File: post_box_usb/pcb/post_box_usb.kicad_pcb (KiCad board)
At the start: 4 copper layers, 90 x 45 mm, 100 parts, among them U1 MCP1700T-3302E/MB, X1 MC146 32768Hz

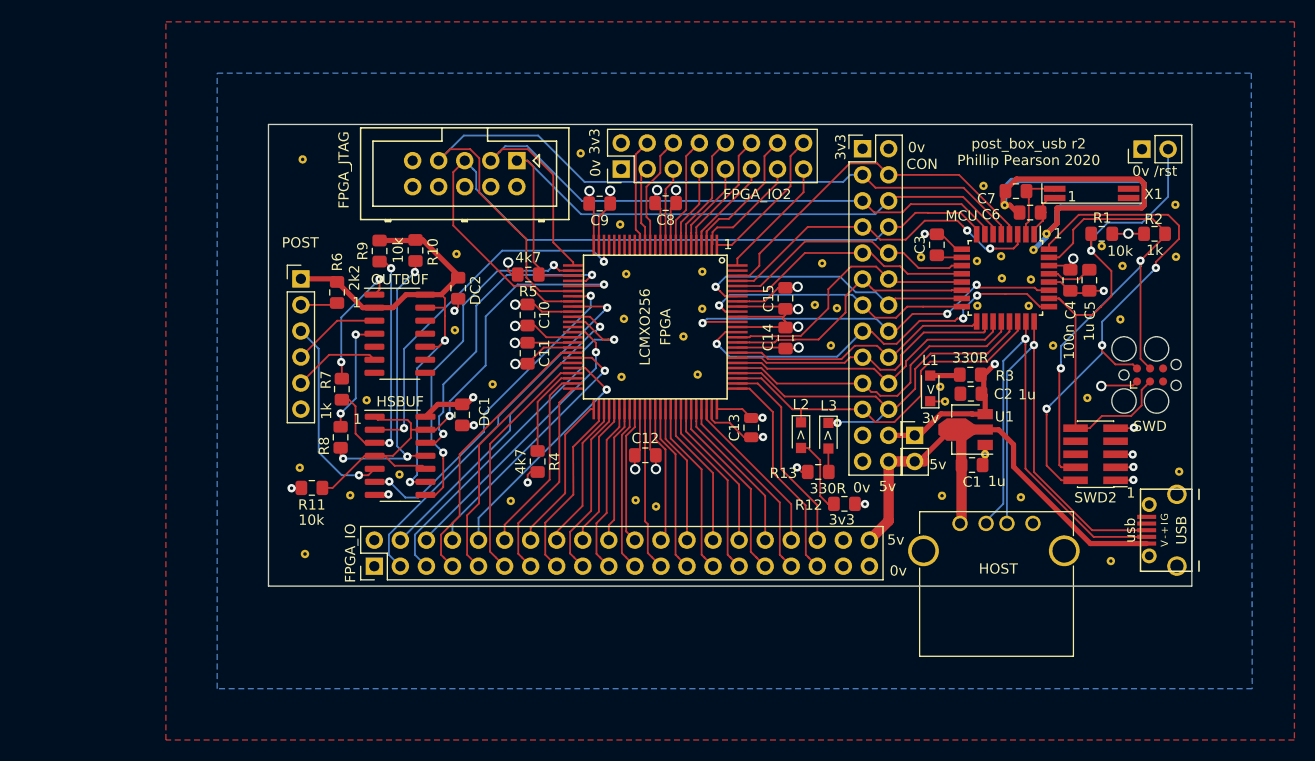
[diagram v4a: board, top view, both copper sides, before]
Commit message: post_box_usb: r2 with an attempt at reverse polarity protection
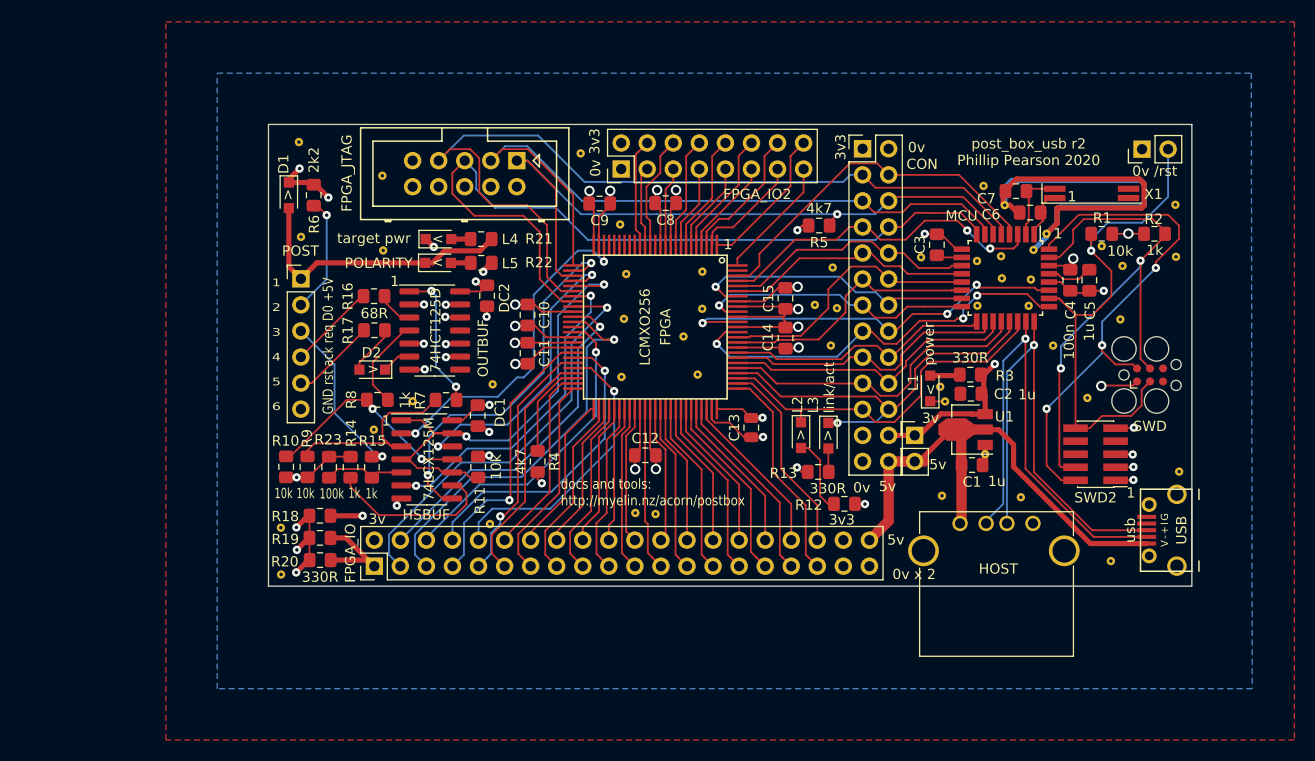
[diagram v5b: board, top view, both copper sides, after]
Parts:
- added D1: BAT54, Diode_SMD:D_SOD-323_HandSoldering, F.Cu at (112.0, 136.9)
- added D2: BAT54, Diode_SMD:D_SOD-323_HandSoldering, F.Cu at (120.1, 153.9)
- added L4: target pwr, Diode_SMD:D_SOD-323_HandSoldering, F.Cu at (126.6, 141.2)
- added L5: POLARITY, Diode_SMD:D_SOD-323_HandSoldering, F.Cu at (126.5, 143.5)
- added R14: 1k, Resistor_SMD:R_0805_2012Metric_Pad1.15x1.40mm_HandSolder, F.Cu at (118.0, 163.4)
- added R15: 1k, Resistor_SMD:R_0805_2012Metric_Pad1.15x1.40mm_HandSolder, F.Cu at (120.1, 163.4)
- added R16: 68R, Resistor_SMD:R_0805_2012Metric_Pad1.15x1.40mm_HandSolder, F.Cu at (120.3, 146.7)
- added R17: 68R, Resistor_SMD:R_0805_2012Metric_Pad1.15x1.40mm_HandSolder, F.Cu at (120.3, 150.1)
- added R18: 330R, Resistor_SMD:R_0805_2012Metric_Pad1.15x1.40mm_HandSolder, F.Cu at (115.0, 168.1)
- added R19: 330R, Resistor_SMD:R_0805_2012Metric_Pad1.15x1.40mm_HandSolder, F.Cu at (115.0, 170.3)
- added R20: 330R, Resistor_SMD:R_0805_2012Metric_Pad1.15x1.40mm_HandSolder, F.Cu at (115.0, 172.5)
- added R21: 330R, Resistor_SMD:R_0805_2012Metric_Pad1.15x1.40mm_HandSolder, F.Cu at (130.7, 141.2)
- added R22: 330R, Resistor_SMD:R_0805_2012Metric_Pad1.15x1.40mm_HandSolder, F.Cu at (130.7, 143.5)
- added R23: 100k, Resistor_SMD:R_0805_2012Metric_Pad1.15x1.40mm_HandSolder, F.Cu at (115.9, 163.4)
- L1: value led -> power
- L3: value led -> link/act
- moved staple_single25 31.7 mm to (113.0, 131.7)
- moved R5 28.8 mm to (163.7, 139.9)
- moved R10 24.6 mm to (111.7, 163.4), turned to 270 degrees
- moved R9 22.2 mm to (113.8, 163.4), turned to 270 degrees
- moved staple_single24 18.9 mm to (111.2, 173.9)
- moved R11 16.3 mm to (130.4, 163.4), turned to 90 degrees
- moved staple_single33 15.3 mm to (113.2, 141.0)
- moved staple_single28 11.0 mm to (124.0, 157.0)
- moved staple_single32 10.5 mm to (121.2, 142.3)
- moved R7 10.2 mm to (127.3, 156.9), turned to 0 degrees
- moved R6 9.75 mm to (114.4, 136.9)
- moved staple_single23 7.93 mm to (121.1, 135.0)
- moved R8 5.12 mm to (120.6, 156.8), turned to 0 degrees
- moved staple_single31 5.03 mm to (120.3, 159.8)
- moved staple_single21 3.48 mm to (111.2, 169.3)
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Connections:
- DC2 pad 1: GND -> target_GND
- HSBUF pad 5: testreq -> target_testreq
- HSBUF pad 9: target_5V -> target_5V_r
- OUTBUF pad 12: GND -> target_GND
- OUTBUF pad 3: testack -> target_testack
- OUTBUF pad 5: GND -> target_GND
- OUTBUF pad 7: GND -> target_GND
- OUTBUF pad 9: GND -> target_GND
- POST pad 1: target_5V -> target_5V_ext
- POST pad 3: testreq -> target_testreq_ext
- POST pad 4: testack -> target_testack_ext
- POST pad 5: target_reset -> target_reset_ext
- POST pad 6: GND -> target_GND
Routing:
- net target_5V: track 52.5 -> 22.8 mm, vias 2 -> 7
- net target_5V_ext: track 0.00 -> 27.6 mm
- net testreq: track 19.2 -> 0.00 mm, vias 1 -> 0
- net target_GND: track 0.00 -> 18.8 mm, vias 0 -> 10
- net target_testreq_ext: track 0.00 -> 17.0 mm, vias 0 -> 1
- net target_5V_r: track 0.00 -> 16.6 mm
- net GND: track 132.3 -> 143.1 mm
- net target_reset_noe_buf: track 29.5 -> 20.7 mm, vias 3 -> 2
- net testack: track 8.63 -> 0.00 mm
- net target_testack_ext: track 0.00 -> 8.56 mm
- net target_reset_ext: track 0.00 -> 8.31 mm
- net target_testreq: track 0.00 -> 7.96 mm
- net target_D0: track 3.60 -> 11.4 mm, vias 0 -> 1
- net testack_noe_buf: track 26.4 -> 19.1 mm, vias 2 -> 0
- net target_reset: track 8.51 -> 2.89 mm
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- added copper zone on In2.Cu, net target_5V
- added copper zone on In1.Cu, net target_GND
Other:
- board text added: "0v x 2"
- board text added: "1 2 3 4 5 6"
- board text added: "<"
- board text added: "GND rst ack req D0 +5V"
- board text added: "docs and tools: http://myelin.nz/acorn/postbox"
- board text added: "post_box_usb r2 Copyright 2017-2020 Google Inc Designed by Phillip Pearson github.com/google/myelin-acorn-electron-hardware myelin.nz/acorn/postbox"
- board text removed: "post_box_usb r1 Copyright 2017-2020 Google Inc Designed by Phillip Pearson github.com/google/myelin-acorn-electron-hardware myelin.nz/acorn/postbox"

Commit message: post_box_usb: r3 candidate; resistors tweaked, diode replaced with mosfet, footprints fixed, test points added
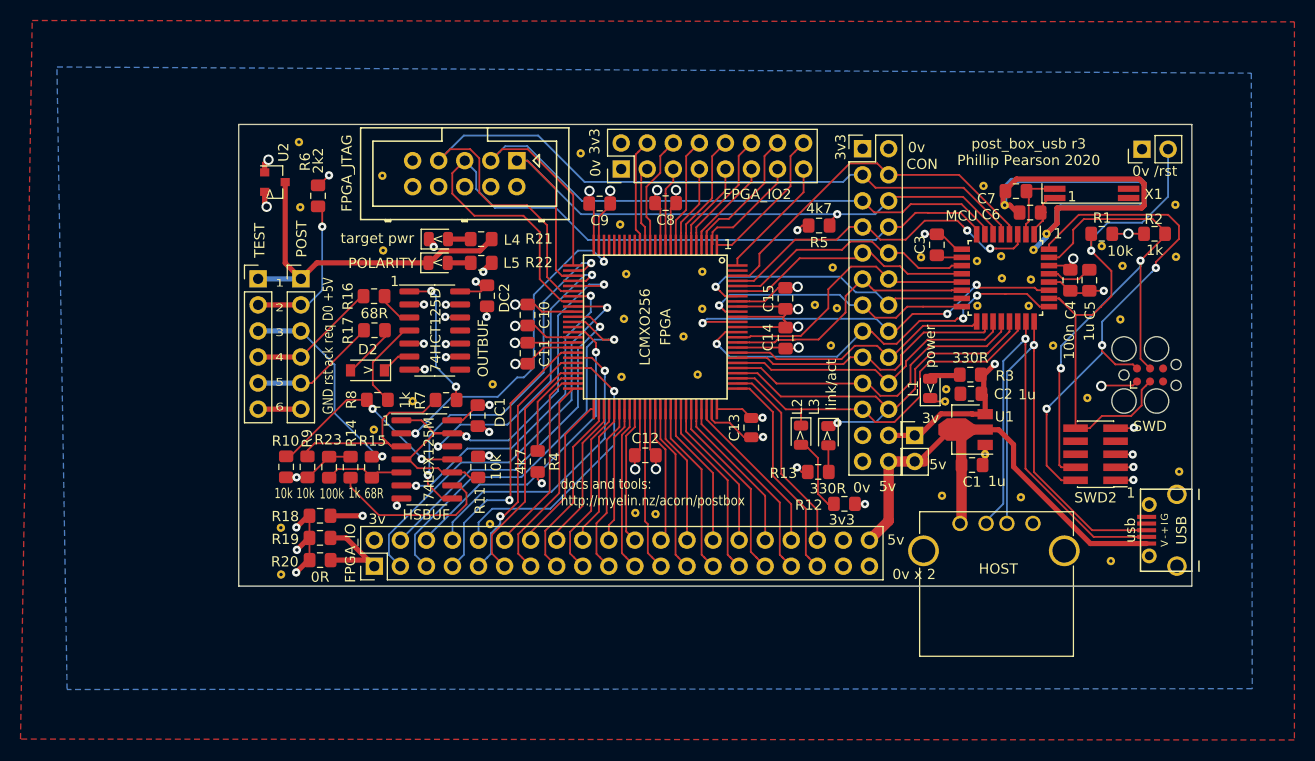
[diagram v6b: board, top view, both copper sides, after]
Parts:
- removed D1: BAT54, Diode_SMD:D_SOD-323_HandSoldering
- added TEST: pins, Connector_PinHeader_2.54mm:PinHeader_1x06_P2.54mm_Vertical, F.Cu at (109.0, 145.1)
- added U2: PMV65XP,215, Package_TO_SOT_SMD:SOT-23, F.Cu at (110.6, 135.6)
- D2: footprint Diode_SMD:D_SOD-323_HandSoldering -> Diode_SMD:D_SOD-123
- L1, L2, L3, L4, L5: footprint Diode_SMD:D_SOD-323_HandSoldering -> LED_SMD:LED_0805_2012Metric
- R15: value 1k -> 68R
- R20: value 330R -> 0R
- moved staple_single33 2.89 mm to (113.1, 138.1)
- moved staple_single20 0.63 mm to (176.1, 155.8)
- moved D2 0.47 mm to (119.7, 154.0)
- moved R6 0.42 mm to (114.8, 137.0)
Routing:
- net target_5V_ext: track 27.6 -> 34.4 mm
- net target_GND: track 18.8 -> 24.2 mm, vias 10 -> 11
- net target_testreq_ext: track 17.0 -> 21.2 mm
- net target_testack_ext: track 8.56 -> 12.7 mm
- net target_reset_ext: track 8.31 -> 12.5 mm
- net target_D0: track 11.4 -> 15.2 mm
- net target_5V: track 22.8 -> 19.5 mm
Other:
- board size 90 x 45 mm -> 92.9 x 45 mm
- board text added: "post_box_usb r3 Copyright 2017-2020 Google Inc Designed by Phillip Pearson github.com/google/myelin-acorn-electron-hardware myelin.nz/acorn/postbox"
- board text added: "post_box_usb r3 Phillip Pearson 2020"
- board text removed: "post_box_usb r2 Copyright 2017-2020 Google Inc Designed by Phillip Pearson github.com/google/myelin-acorn-electron-hardware myelin.nz/acorn/postbox"
- board text removed: "post_box_usb r2 Phillip Pearson 2020"

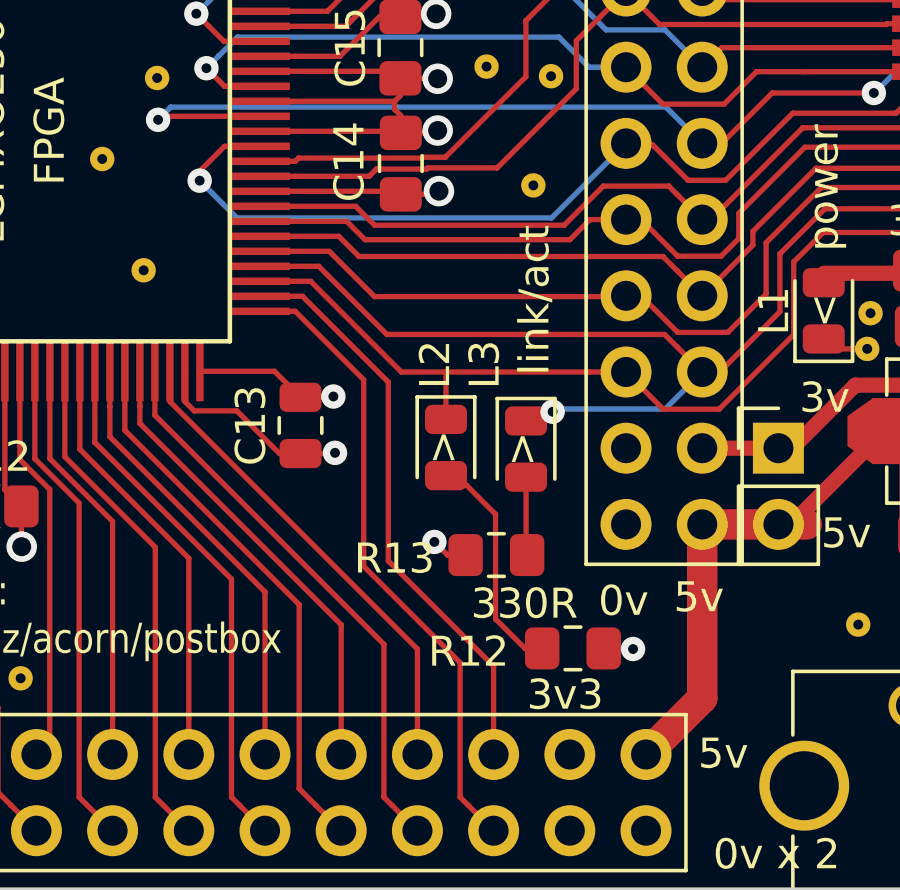
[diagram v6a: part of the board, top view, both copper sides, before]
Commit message: post_box_usb: Replaced L2 with an WS2812-V5
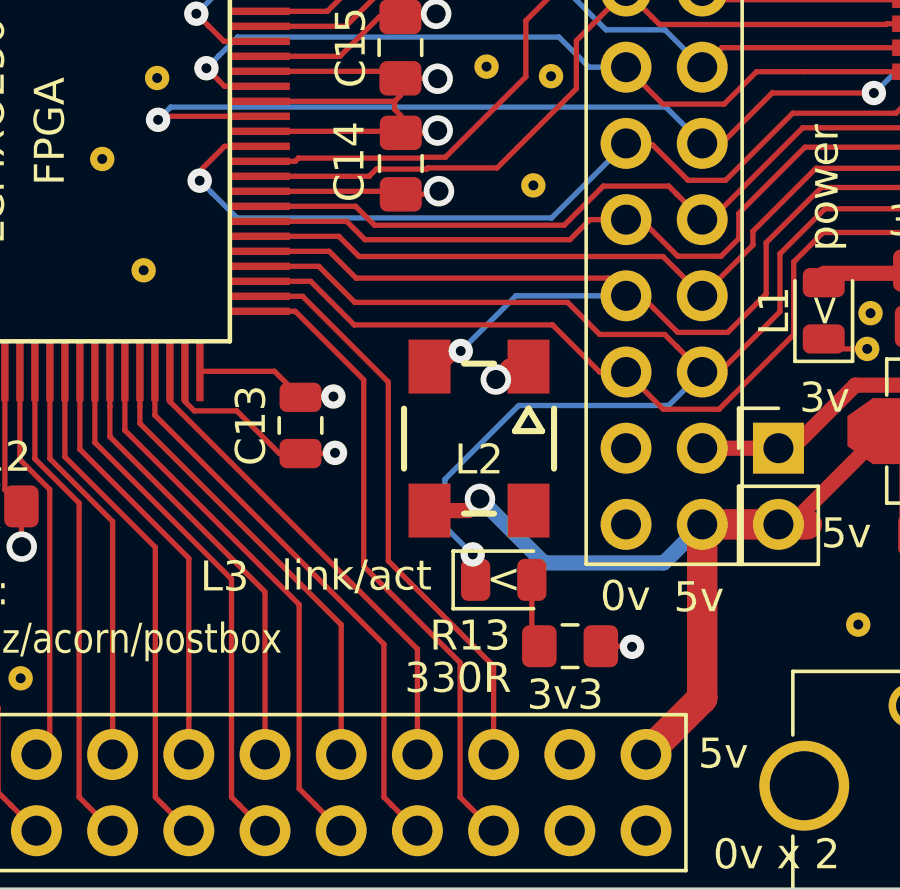
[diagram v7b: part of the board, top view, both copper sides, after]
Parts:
- removed R12: 330R, Resistor_SMD:R_0805_2012Metric_Pad1.15x1.40mm_HandSolder
- L2: value led -> WS2812B-V5; footprint LED_SMD:LED_0805_2012Metric -> myelin-kicad:WS2812B_PP
- R18, R19: value 330R -> 0R NF
- moved L3 4.42 mm to (163.8, 164.7), turned to 0 degrees
- moved R13 3.91 mm to (166.0, 166.9), turned to 180 degrees
- moved L2 1.14 mm to (163.0, 160.0), turned to 0 degrees
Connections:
- L2 pad 1: mcu_RXD -> 5V
- L2 pad 2: mcu_txd_led_anode -> (no net)
- L3 pad 2: mcu_rxd_led_anode -> mcu_txd_led_anode
- R13 pad 2: mcu_rxd_led_anode -> mcu_txd_led_anode
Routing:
- net 5V: track 51.3 -> 62.0 mm, vias 0 -> 1
- net PA19: track 31.4 -> 38.9 mm, vias 0 -> 1
- net mcu_TXD: track 39.7 -> 47.1 mm
- net mcu_txd_led_anode: track 7.51 -> 2.31 mm
- net mcu_rxd_led_anode: track 2.30 -> 0.00 mm
- net mcu_RXD: track 36.4 -> 35.1 mm
- net GND: track 143.1 -> 144.4 mm, vias 16 -> 17
- net 3V3: track 95.6 -> 94.5 mm, vias 19 -> 18

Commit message: It's 2021; added JLC order no placeholder; r3 release candidate
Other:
- board text added: "JLCJLCJLCJLC"
- board text added: "post_box_usb r3 Copyright 2017-2021 Google Inc Designed by Phillip Pearson myelin.nz/acorn/postbox"
- board text added: "post_box_usb r3 Phillip Pearson 2021"
- board text removed: "post_box_usb r3 Copyright 2017-2020 Google Inc Designed by Phillip Pearson github.com/google/myelin-acorn-electron-hardware myelin.nz/acorn/postbox"
- board text removed: "post_box_usb r3 Phillip Pearson 2020"
